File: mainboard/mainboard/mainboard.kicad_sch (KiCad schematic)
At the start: 7 parts

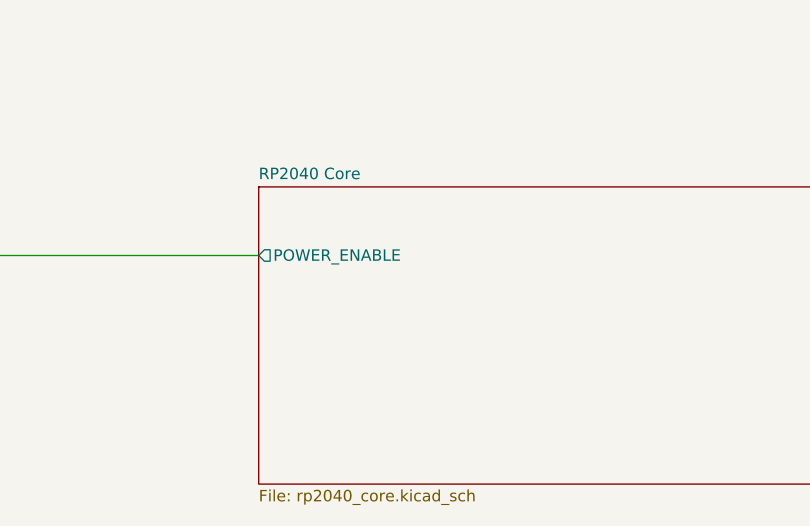
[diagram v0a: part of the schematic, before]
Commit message: Rename KiCad files and sheets to match what they contain
- mainboard: rp2040_core.kicad_sch -> rp2350_core.kicad_sch and the
  sheet "RP2040 Core" -> "RP2350 Core"; the sheet holds the RP2350.
  Hierarchical net names, footprint sheet properties and the net-class
  patterns in the .kicad_pro follow the new sheet name.
- gpu_vga_extension, gpu_dvi_card: both projects were still called
  gpu_extension; name each after its directory, including the
  (project ...) instance blocks in every sheet.
- gpu_vga_extension: dvi.kicad_sch -> vga.kicad_sch and the sheet
  "DVI connector" -> "VGA connector"; it holds the VGA connector and DAC.
- bus_adapter_20pin: the project inside was bus_adapter_10pin; rename
  the directory and files to bus_adapter_20pin.

kicad-cli ERC and DRC with schematic parity give the same entries before
and after (names aside) for all four projects. Existing gerbers keep
their old file names until the boards are plotted again.

Co-Authored-By: Claude Opus 5 (1M context) <noreply@anthropic.com>
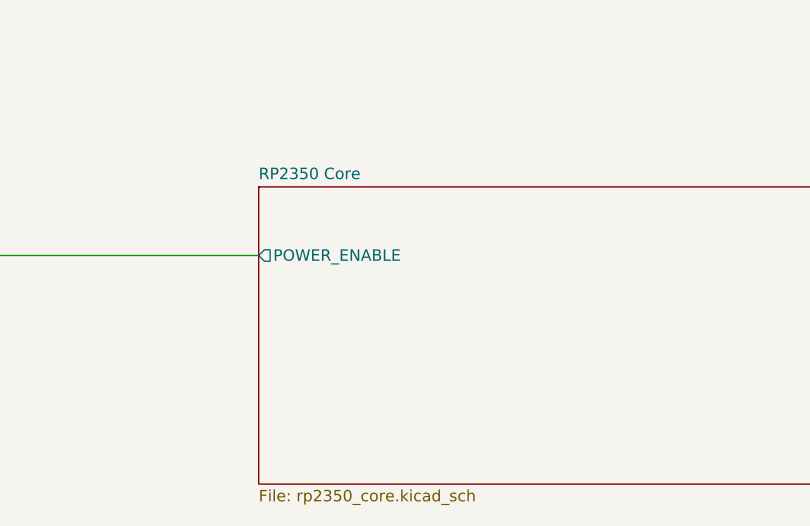
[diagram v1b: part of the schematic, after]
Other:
- sheet RP2040 Core renamed RP2350 Core
- sheet RP2350 Core: file rp2040_core.kicad_sch -> rp2350_core.kicad_sch
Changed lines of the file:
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@@
 			(color 0 0 0 0.0000)
 		)
-		(property "Sheetname" "RP2040 Core"
+		(property "Sheetname" "RP2350 Core"
 			(at 114.3 78.0284 0)
 			(effects
@@
 			)
 		)
-		(property "Sheetfile" "rp2040_core.kicad_sch"
+		(property "Sheetfile" "rp2350_core.kicad_sch"
 			(at 114.3 112.3446 0)
 			(effects
